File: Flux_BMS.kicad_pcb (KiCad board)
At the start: 2 copper layers, 73.2 x 57.4 mm, 12 parts, among them Q1 BSS84, Q2 BSS84, U1 LTC6811-1

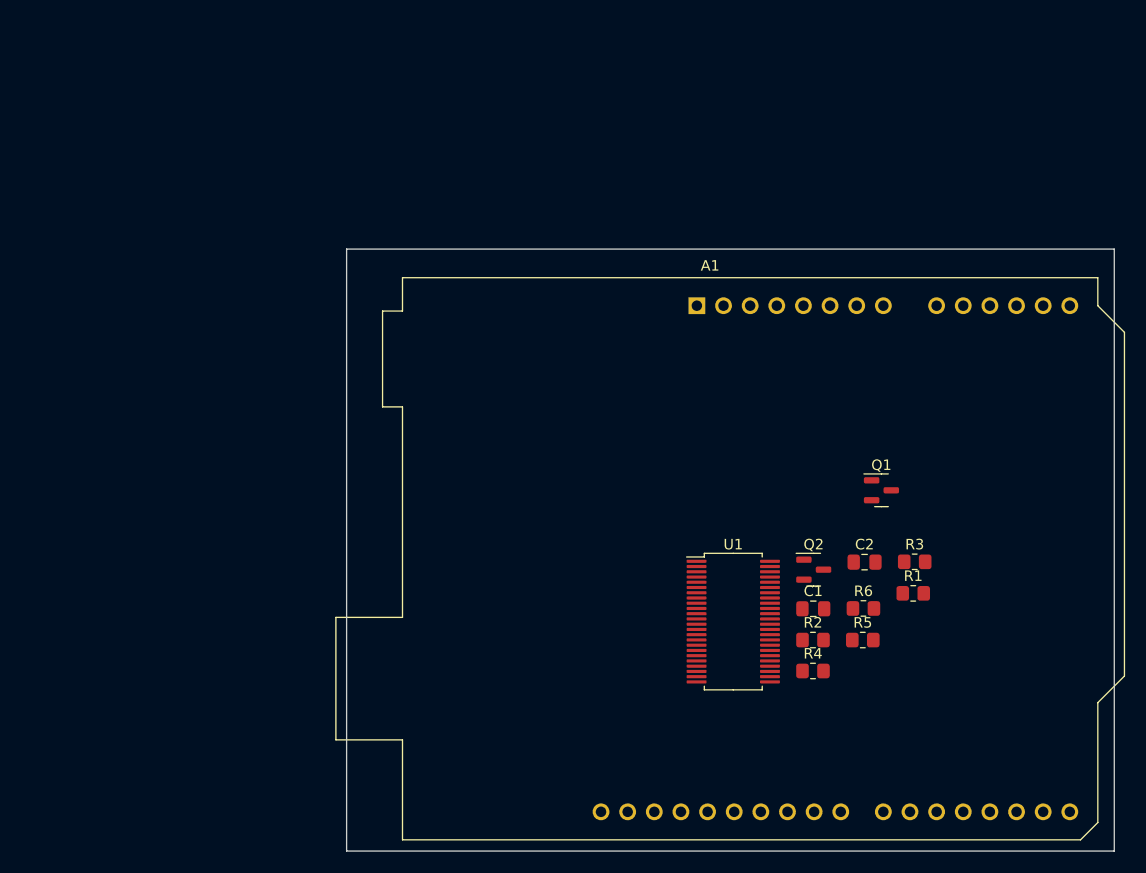
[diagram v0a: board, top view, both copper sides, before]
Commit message: Added ltc6811
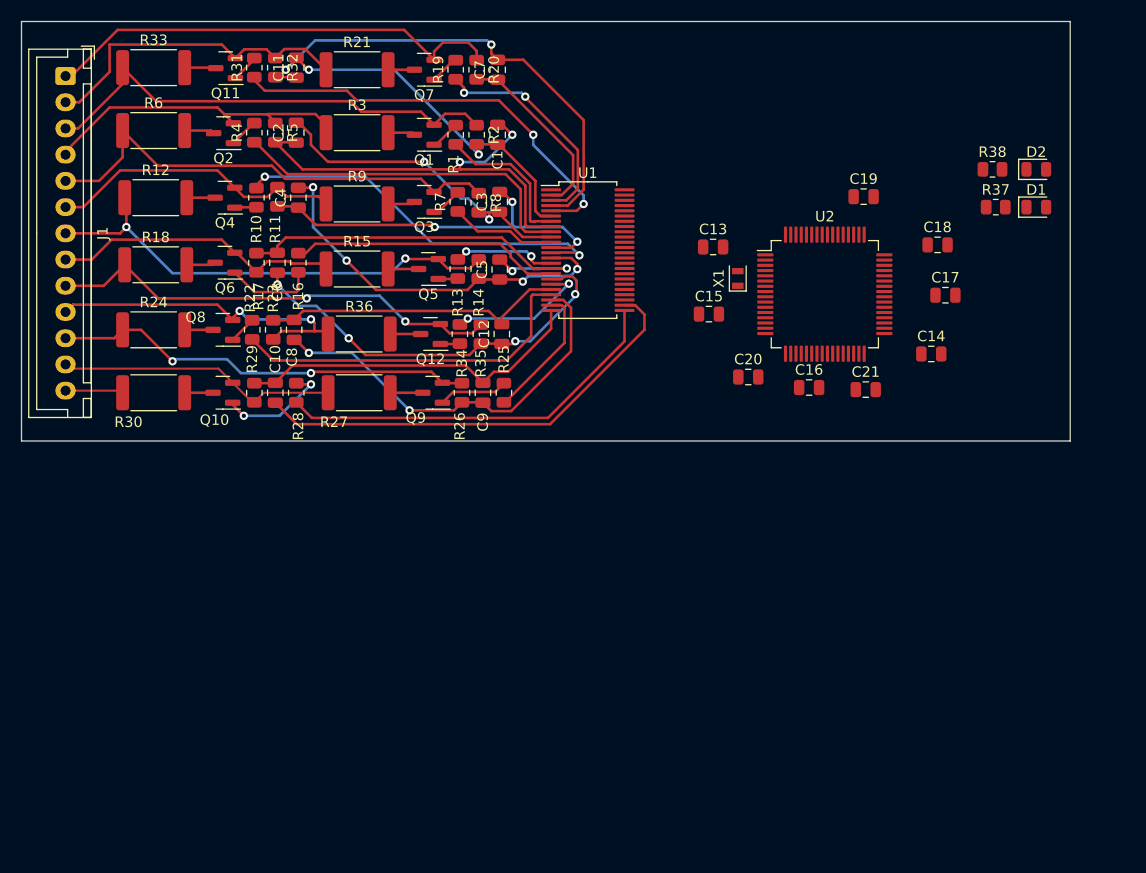
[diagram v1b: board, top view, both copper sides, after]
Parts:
- removed A1: Arduino_UNO_R3, Module:Arduino_UNO_R3
- added C10: 10n, Capacitor_SMD:C_0805_2012Metric, F.Cu at (99.2, 85.4)
- added C11: 10n, Capacitor_SMD:C_0805_2012Metric, F.Cu at (101.2, 54.4)
- added C12: 10n, Capacitor_SMD:C_0805_2012Metric, F.Cu at (120.8, 79.8)
- added C13: 20p, Capacitor_SMD:C_0805_2012Metric, F.Cu at (140.9, 71.5)
- added C14: 100n, Capacitor_SMD:C_0805_2012Metric, F.Cu at (161.8, 81.7)
- added C15: 20p, Capacitor_SMD:C_0805_2012Metric, F.Cu at (140.6, 77.9)
- added C16: 100n, Capacitor_SMD:C_0805_2012Metric, F.Cu at (150.1, 84.9)
- added C17: 100n, Capacitor_SMD:C_0805_2012Metric, F.Cu at (163.1, 76.1)
- added C18: 100n, Capacitor_SMD:C_0805_2012Metric, F.Cu at (162.3, 71.3)
- added C19: 4,7u, Capacitor_SMD:C_0805_2012Metric, F.Cu at (155.3, 66.7)
- added C20: 100n, Capacitor_SMD:C_0805_2012Metric, F.Cu at (144.3, 83.9)
- added C21: 1u, Capacitor_SMD:C_0805_2012Metric, F.Cu at (155.5, 85.1)
- added C3: 10n, Capacitor_SMD:C_0805_2012Metric, F.Cu at (120.6, 67.2)
- added C4: 10n, Capacitor_SMD:C_0805_2012Metric, F.Cu at (101.4, 66.8)
- added C5: 10n, Capacitor_SMD:C_0805_2012Metric, F.Cu at (120.6, 73.7)
- added C6: 10n, Capacitor_SMD:C_0805_2012Metric, F.Cu at (99.4, 73.0)
- added C7: 10n, Capacitor_SMD:C_0805_2012Metric, F.Cu at (120.4, 54.6)
- added C8: 10n, Capacitor_SMD:C_0805_2012Metric, F.Cu at (101.0, 79.4)
- added C9: 10n, Capacitor_SMD:C_0805_2012Metric, F.Cu at (119.0, 85.4)
- added D1: RED, LED_SMD:LED_0805_2012Metric, F.Cu at (171.8, 67.7)
- added D2: GREEN, LED_SMD:LED_0805_2012Metric, F.Cu at (171.8, 64.1)
- added J1: Conn_01x13, Connector_JST:JST_XH_B13B-XH-A_1x13_P2.50mm_Vertical, F.Cu at (79.2, 55.2)
- added Q10: BSS84, Package_TO_SOT_SMD:SOT-23, F.Cu at (94.2, 85.4)
- added Q11: BSS84, Package_TO_SOT_SMD:SOT-23, F.Cu at (94.5, 54.5)
- added Q12: BSS84, Package_TO_SOT_SMD:SOT-23, F.Cu at (114.0, 79.8)
- added Q3: BSS84, Package_TO_SOT_SMD:SOT-23, F.Cu at (113.4, 67.2)
- added Q4: BSS84, Package_TO_SOT_SMD:SOT-23, F.Cu at (94.4, 66.8)
- added Q5: BSS84, Package_TO_SOT_SMD:SOT-23, F.Cu at (113.8, 73.6)
- added Q6: BSS84, Package_TO_SOT_SMD:SOT-23, F.Cu at (94.4, 73.0)
- added Q7: BSS84, Package_TO_SOT_SMD:SOT-23, F.Cu at (113.4, 54.6)
- added Q8: BSS84, Package_TO_SOT_SMD:SOT-23, F.Cu at (94.2, 79.4)
- added Q9: BSS84, Package_TO_SOT_SMD:SOT-23, F.Cu at (114.2, 85.4)
- added R10: 3k3, Resistor_SMD:R_0805_2012Metric, F.Cu at (97.4, 66.8)
- added R11: 100, Resistor_SMD:R_0805_2012Metric, F.Cu at (99.4, 66.7)
- added R12: 33, Resistor_SMD:R_2512_6332Metric, F.Cu at (87.8, 66.8)
- added R13: 3k3, Resistor_SMD:R_0805_2012Metric, F.Cu at (116.6, 73.6)
- added R14: 100, Resistor_SMD:R_0805_2012Metric, F.Cu at (118.6, 73.6)
- added R15: 33, Resistor_SMD:R_2512_6332Metric, F.Cu at (107.0, 73.6)
- added R16: 3k3, Resistor_SMD:R_0805_2012Metric, F.Cu at (101.4, 73.0)
- added R17: 100, Resistor_SMD:R_0805_2012Metric, F.Cu at (97.4, 73.0)
- added R18: 33, Resistor_SMD:R_2512_6332Metric, F.Cu at (87.8, 73.2)
- added R19: 3k3, Resistor_SMD:R_0805_2012Metric, F.Cu at (116.4, 54.6)
- added R20: 100, Resistor_SMD:R_0805_2012Metric, F.Cu at (118.4, 54.6)
- added R21: 33, Resistor_SMD:R_2512_6332Metric, F.Cu at (107.0, 54.6)
- added R22: 3k3, Resistor_SMD:R_0805_2012Metric, F.Cu at (97.0, 79.4)
- added R23: 100, Resistor_SMD:R_0805_2012Metric, F.Cu at (99.0, 79.4)
- added R24: 33, Resistor_SMD:R_2512_6332Metric, F.Cu at (87.6, 79.4)
- added R25: 3k3, Resistor_SMD:R_0805_2012Metric, F.Cu at (121.0, 85.4)
- added R26: 100, Resistor_SMD:R_0805_2012Metric, F.Cu at (117.0, 85.4)
- added R27: 33, Resistor_SMD:R_2512_6332Metric, F.Cu at (107.2, 85.4)
- added R28: 3k3, Resistor_SMD:R_0805_2012Metric, F.Cu at (101.2, 85.4)
- added R29: 100, Resistor_SMD:R_0805_2012Metric, F.Cu at (97.2, 85.4)
- added R30: 33, Resistor_SMD:R_2512_6332Metric, F.Cu at (87.6, 85.4)
- added R31: 3k3, Resistor_SMD:R_0805_2012Metric, F.Cu at (97.2, 54.4)
- added R32: 100, Resistor_SMD:R_0805_2012Metric, F.Cu at (99.2, 54.4)
- added R33: 33, Resistor_SMD:R_2512_6332Metric, F.Cu at (87.6, 54.4)
- added R34: 3k3, Resistor_SMD:R_0805_2012Metric, F.Cu at (116.8, 79.8)
- added R35: 100, Resistor_SMD:R_0805_2012Metric, F.Cu at (118.8, 79.8)
- added R36: 33, Resistor_SMD:R_2512_6332Metric, F.Cu at (107.2, 79.8)
- added R37: 100, Resistor_SMD:R_0805_2012Metric, F.Cu at (167.9, 67.7)
- added R38: 100, Resistor_SMD:R_0805_2012Metric, F.Cu at (167.6, 64.1)
- added R7: 3k3, Resistor_SMD:R_0805_2012Metric, F.Cu at (116.6, 67.2)
- added R8: 100, Resistor_SMD:R_0805_2012Metric, F.Cu at (118.6, 67.3)
- added R9: 33, Resistor_SMD:R_2512_6332Metric, F.Cu at (107.0, 67.4)
- added U2: STM32L476RGTx, Package_QFP:LQFP-64_10x10mm_P0.5mm, F.Cu at (151.6, 76.0)
- added X1: 8MHz(16pF), Crystal:Crystal_SMD_2012-2Pin_2.0x1.2mm, F.Cu at (143.3, 74.5)
- C1, C2: footprint Capacitor_SMD:C_0805_2012Metric_Pad1.18x1.45mm_HandSolder -> Capacitor_SMD:C_0805_2012Metric
- R1, R2, R4: footprint Resistor_SMD:R_0805_2012Metric_Pad1.20x1.40mm_HandSolder -> Resistor_SMD:R_0805_2012Metric
- R3: value 100 -> 33; footprint Resistor_SMD:R_0805_2012Metric_Pad1.20x1.40mm_HandSolder -> Resistor_SMD:R_2512_6332Metric
- R5: value 33 -> 100; footprint Resistor_SMD:R_0805_2012Metric_Pad1.20x1.40mm_HandSolder -> Resistor_SMD:R_0805_2012Metric
- R6: footprint Resistor_SMD:R_0805_2012Metric_Pad1.20x1.40mm_HandSolder -> Resistor_SMD:R_2512_6332Metric
- moved R6 81.6 mm to (87.6, 60.4)
- moved R5 74.0 mm to (99.2, 60.6), turned to -90 degrees
- moved R4 74.0 mm to (97.2, 60.6), turned to 90 degrees
- moved Q2 70.0 mm to (94.3, 60.6), turned to 180 degrees
- moved C2 67.9 mm to (101.2, 60.6), turned to 90 degrees
- moved R3 67.1 mm to (107.0, 60.6)
- moved R1 61.8 mm to (116.4, 60.8), turned to 90 degrees
- moved R2 57.9 mm to (118.4, 60.8), turned to -90 degrees
- moved Q1 55.2 mm to (113.4, 60.8), turned to 180 degrees
- moved C1 54.3 mm to (120.4, 60.8), turned to 90 degrees
- moved U1 38.0 mm to (129.0, 71.8)
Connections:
- C1 pad 1: Net-(U1-Pad2) -> /LTC6811/SENSE+_10
- C1 pad 2: Net-(U1-Pad4) -> /LTC6811/SENSE+_9
- C2 pad 1: Net-(U1-Pad4) -> /LTC6811/SENSE+_9
- C2 pad 2: Net-(U1-Pad6) -> /LTC6811/SENSE+_8
- Q1 pad 2: Net-(Q1-Pad2) -> /LTC6811/CELL+_10
- Q2 pad 2: Net-(J1-Pad2) -> /LTC6811/CELL+_9
- R1 pad 1: Net-(U1-Pad3) -> /LTC6811/BALANCE_10
- R2 pad 1: Net-(U1-Pad2) -> /LTC6811/CELL+_10
- R2 pad 2: Net-(Q1-Pad2) -> /LTC6811/SENSE+_10
- R3 pad 1: Net-(U1-Pad4) -> /LTC6811/CELL+_9
- R3 pad 2: Net-(J1-Pad2) -> Net-(Q1-Pad3)
- R4 pad 1: Net-(U1-Pad5) -> /LTC6811/BALANCE_9
- R5 pad 1: Net-(Q2-Pad3) -> /LTC6811/CELL+_9
- R5 pad 2: Net-(Q1-Pad3) -> /LTC6811/SENSE+_9
- R6 pad 1: unconnected-(R6-Pad1) -> /LTC6811/CELL+_8
- U1 pad 10: unconnected-(U1-Pad10) -> /LTC6811/SENSE+_8
- U1 pad 11: unconnected-(U1-Pad11) -> /LTC6811/BALANCE_8
- U1 pad 12: unconnected-(U1-Pad12) -> /LTC6811/SENSE+_7
- U1 pad 13: unconnected-(U1-Pad13) -> /LTC6811/BALANCE_7
- U1 pad 14: unconnected-(U1-Pad14) -> /LTC6811/SENSE+_6
- U1 pad 15: unconnected-(U1-Pad15) -> /LTC6811/BALANCE_6
- U1 pad 16: unconnected-(U1-Pad16) -> /LTC6811/SENSE+_5
- U1 pad 17: unconnected-(U1-Pad17) -> /LTC6811/BALANCE_5
- U1 pad 18: unconnected-(U1-Pad18) -> /LTC6811/SENSE+_4
- U1 pad 19: unconnected-(U1-Pad19) -> /LTC6811/BALANCE_4
- U1 pad 2: Net-(U1-Pad2) -> /LTC6811/SENSE+_12
- U1 pad 20: unconnected-(U1-Pad20) -> /LTC6811/SENSE+_3
- U1 pad 21: unconnected-(U1-Pad21) -> /LTC6811/BALANCE_3
- U1 pad 22: unconnected-(U1-Pad22) -> /LTC6811/SENSE+_2
- U1 pad 23: unconnected-(U1-Pad23) -> /LTC6811/BALANCE_2
- U1 pad 24: unconnected-(U1-Pad24) -> /LTC6811/SENSE+_1
- U1 pad 25: unconnected-(U1-Pad25) -> /LTC6811/BALANCE_1
- U1 pad 26: unconnected-(U1-Pad26) -> /LTC6811/Cell1/SENSE-
- U1 pad 3: Net-(U1-Pad3) -> /LTC6811/BALANCE_12
- U1 pad 4: Net-(U1-Pad4) -> /LTC6811/SENSE+_11
- U1 pad 5: Net-(U1-Pad5) -> /LTC6811/BALANCE_11
- U1 pad 6: Net-(U1-Pad6) -> /LTC6811/SENSE+_10
- U1 pad 7: unconnected-(U1-Pad7) -> /LTC6811/BALANCE_10
- U1 pad 8: unconnected-(U1-Pad8) -> /LTC6811/SENSE+_9
- U1 pad 9: unconnected-(U1-Pad9) -> /LTC6811/BALANCE_9
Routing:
- net /LTC6811/SENSE+_11: track 0.00 -> 46.9 mm, vias 0 -> 2
- net /LTC6811/CELL+_8: track 0.00 -> 46.0 mm
- net /LTC6811/CELL+_10: track 0.00 -> 45.7 mm
- net /LTC6811/CELL+_6: track 0.00 -> 45.6 mm, vias 0 -> 2
- net /LTC6811/CELL+_12: track 0.00 -> 44.6 mm
- net /LTC6811/CELL+_4: track 0.00 -> 43.7 mm, vias 0 -> 2
- net /LTC6811/Cell1/SENSE-: track 0.00 -> 43.5 mm
- net /LTC6811/SENSE+_9: track 0.00 -> 42.5 mm, vias 0 -> 2
- net /LTC6811/BALANCE_11: track 0.00 -> 41.0 mm, vias 0 -> 2
- net /LTC6811/CELL+_2: track 0.00 -> 40.5 mm, vias 0 -> 2
- net /LTC6811/SENSE+_5: track 0.00 -> 39.8 mm, vias 0 -> 2
- net /LTC6811/SENSE+_4: track 0.00 -> 38.9 mm, vias 0 -> 4
- net /LTC6811/SENSE+_2: track 0.00 -> 38.6 mm, vias 0 -> 2
- net /LTC6811/BALANCE_1: track 0.00 -> 37.9 mm
- net /LTC6811/SENSE+_6: track 0.00 -> 37.2 mm, vias 0 -> 4
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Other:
- board size 73.2 x 57.4 mm -> 100 x 40 mm

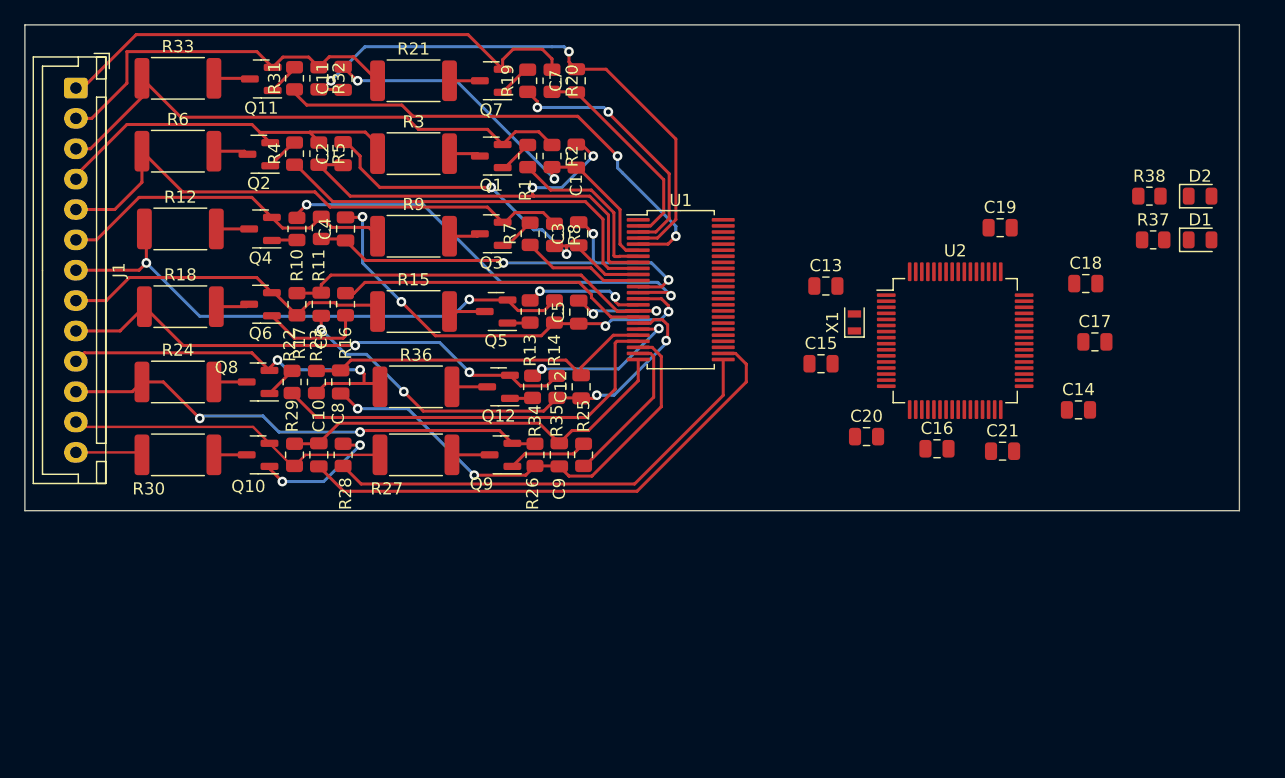
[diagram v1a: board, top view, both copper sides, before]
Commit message: Added part of power schematic
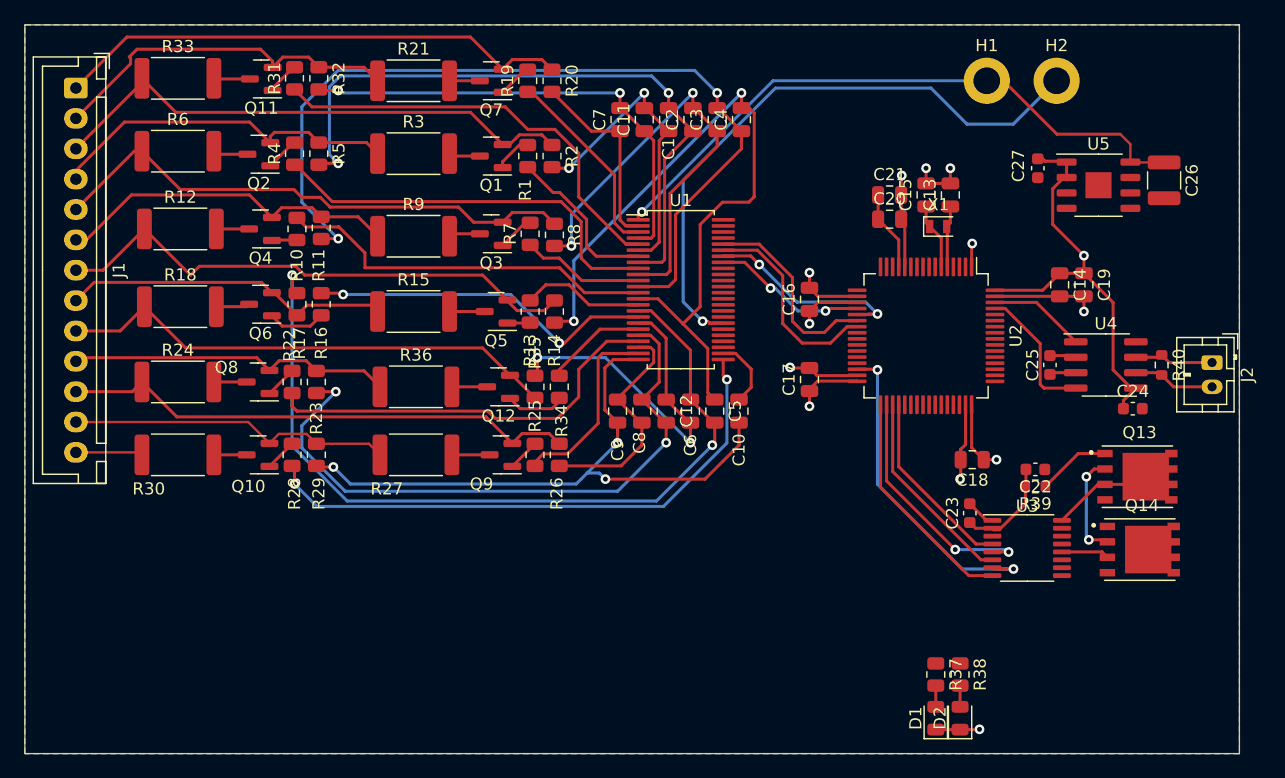
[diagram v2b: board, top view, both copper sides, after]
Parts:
- added C22: 10n, Capacitor_SMD:C_0603_1608Metric, F.Cu at (158.2, 86.6)
- added C23: 470n, Capacitor_SMD:C_0603_1608Metric, F.Cu at (152.8, 90.2)
- added C24: 2u2, Capacitor_SMD:C_0603_1608Metric, F.Cu at (166.2, 81.6)
- added C25: 2u2, Capacitor_SMD:C_0603_1608Metric, F.Cu at (159.4, 78.0)
- added C26: 1u, 63V, Capacitor_SMD:C_1210_3225Metric, F.Cu at (168.8, 62.8)
- added C27: 1u, Capacitor_SMD:C_0603_1608Metric, F.Cu at (158.4, 61.8)
- added H1: MountingHole_Pad, MountingHole:MountingHole_2.2mm_M2_DIN965_Pad, F.Cu at (154.2, 54.6)
- added H2: MountingHole_Pad, MountingHole:MountingHole_2.2mm_M2_DIN965_Pad, F.Cu at (159.9, 54.6)
- added J2: CAN, Connector_JST:JST_PH_B2B-PH-K_1x02_P2.00mm_Vertical, F.Cu at (172.8, 77.8)
- added Q13: Q_NMOS_SDG, FLUX-BMS:TRANS_DMP2002UPS-13, F.Cu at (166.6, 87.2)
- added Q14: Q_NMOS_SDG, FLUX-BMS:TRANS_DMP2002UPS-13, F.Cu at (166.8, 93.2)
- added R39: 100, Resistor_SMD:R_0603_1608Metric, F.Cu at (158.2, 88.0)
- added R40: 220, Resistor_SMD:R_0603_1608Metric, F.Cu at (168.6, 78.0)
- added U3: BQ76200PW, Package_SO:TSSOP-16_4.4x5mm_P0.65mm, F.Cu at (157.5, 93.1)
- added U4: TJA1051T-3, Package_SO:SOIC-8_3.9x4.9mm_P1.27mm, F.Cu at (164.0, 78.0)
- added U5: RT9068, FLUX-BMS:SOP-8_3.9x4.9mm_P1.27mm_with_therma, F.Cu at (163.4, 63.2)
- moved D2 47.3 mm to (152.0, 107.1), turned to 90 degrees
- moved D1 45.0 mm to (150.0, 107.1), turned to 90 degrees
- moved R38 42.4 mm to (152.0, 103.5), turned to -90 degrees
- moved R37 40.0 mm to (150.0, 103.5), turned to -90 degrees
- moved C10 34.8 mm to (133.8, 81.8), turned to 90 degrees
- moved C4 33.8 mm to (134.0, 57.8)
- moved C6 31.6 mm to (129.8, 81.8)
- moved C2 28.9 mm to (130.0, 57.8)
- moved C11 25.0 mm to (126.0, 57.8)
- moved C8 24.9 mm to (125.8, 81.8)
- moved C17 23.7 mm to (139.6, 79.2), turned to 90 degrees
- moved C21 23.1 mm to (146.2, 64.0)
- moved C20 18.0 mm to (146.2, 66.0)
- moved C18 17.3 mm to (153.0, 85.8), turned to 180 degrees
- moved C15 16.4 mm to (149.2, 64.0), turned to 90 degrees
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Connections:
- net LED_GREEN renamed /STM32L476/LED_GREEN
- net LED_RED renamed /STM32L476/LED_RED
- net Net-(U1-Pad30) renamed V-
- net VDD renamed +3V3
- U1 pad 1: unconnected-(U1-Pad1) -> V+
- U1 pad 41: unconnected-(U1-Pad41) -> /LTC6811/LTC_CS
- U1 pad 42: unconnected-(U1-Pad42) -> /LTC6811/LTC_SCK
- U1 pad 43: unconnected-(U1-Pad43) -> /LTC6811/LTC_SDI
- U1 pad 44: unconnected-(U1-Pad44) -> /LTC6811/LTC_SDO
- U2 pad 20: unconnected-(U2-Pad20) -> /LTC6811/LTC_CS
- U2 pad 21: unconnected-(U2-Pad21) -> /LTC6811/LTC_SCK
- U2 pad 22: unconnected-(U2-Pad22) -> /LTC6811/LTC_SDO
- U2 pad 23: unconnected-(U2-Pad23) -> /LTC6811/LTC_SDI
- U2 pad 30: unconnected-(U2-Pad30) -> /Charge_control/BQ_PMON_EN
- U2 pad 33: unconnected-(U2-Pad33) -> /Charge_control/BQ_PCHG_EN
- U2 pad 34: unconnected-(U2-Pad34) -> /Charge_control/BQ_CP_EN
- U2 pad 35: unconnected-(U2-Pad35) -> /Charge_control/BQ_DSG_EN
- U2 pad 36: unconnected-(U2-Pad36) -> /Charge_control/BQ_CHG_EN
- U2 pad 61: unconnected-(U2-Pad61) -> /CAN/CAN_RX
- U2 pad 62: unconnected-(U2-Pad62) -> /CAN/CAN_TX
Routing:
- net +3V3: track 0.00 -> 102.8 mm, vias 0 -> 5
- net V+: track 0.00 -> 51.9 mm, vias 0 -> 1
- net V-: track 0.00 -> 50.7 mm, vias 0 -> 1
- net GND: track 0.00 -> 44.1 mm, vias 0 -> 8
- net /LTC6811/Cell1/SENSE-: track 43.5 -> 5.76 mm
- net /LTC6811/SENSE+_7: track 36.8 -> 71.5 mm, vias 3 -> 2
- net /LTC6811/SENSE+_5: track 39.8 -> 68.5 mm
- net /Charge_control/BQ_PMON_EN: track 0.00 -> 27.0 mm, vias 0 -> 2
- net /LTC6811/SENSE+_6: track 37.2 -> 61.5 mm, vias 4 -> 2
- net /LTC6811/SENSE+_3: track 29.1 -> 52.2 mm, vias 0 -> 2
- net /Charge_control/BQ_CP_EN: track 0.00 -> 20.1 mm, vias 0 -> 2
- net /LTC6811/SENSE+_2: track 38.6 -> 18.8 mm, vias 2 -> 0
- net /Charge_control/BQ_PCHG_EN: track 0.00 -> 19.0 mm
- net /LTC6811/SENSE+_1: track 33.6 -> 52.2 mm, vias 0 -> 3
- net /LTC6811/LTC_SCK: track 0.00 -> 17.2 mm, vias 0 -> 2
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- added copper zone on B.Cu, net GND
- added copper zone on F.Cu, net GND
- added copper zone on In1.Cu, net GND
- added copper zone on In2.Cu, net GND
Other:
- board size 100 x 40 mm -> 100 x 60 mm
- copper layers 2 -> 4
